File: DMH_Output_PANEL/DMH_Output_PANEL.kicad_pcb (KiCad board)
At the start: 2 copper layers, 50 x 200 mm, 17 parts, among them J0 Panel_GND_Solder_Wire_Pad

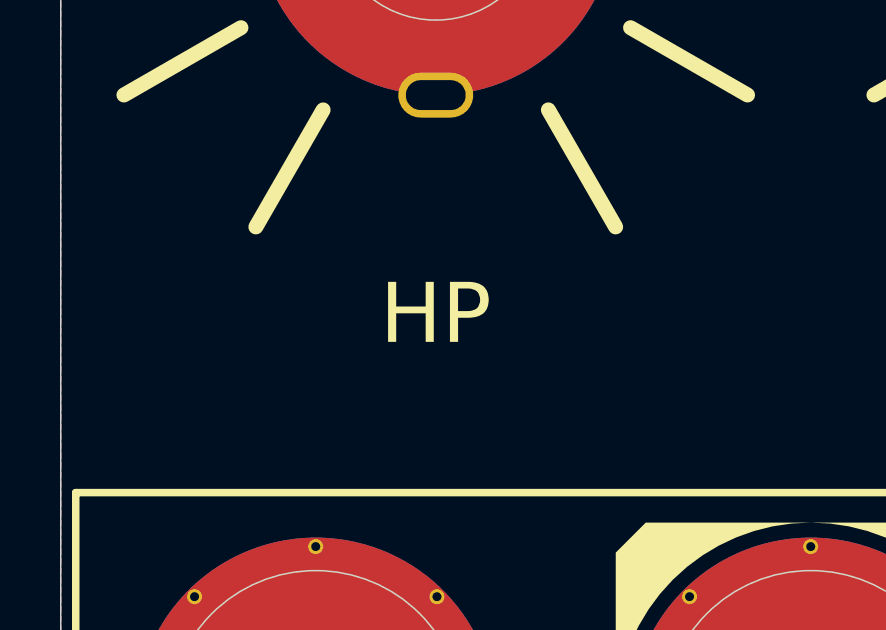
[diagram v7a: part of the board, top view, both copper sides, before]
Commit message: Generated Gerbers for prototyping
Panel, Controls and LEDs only
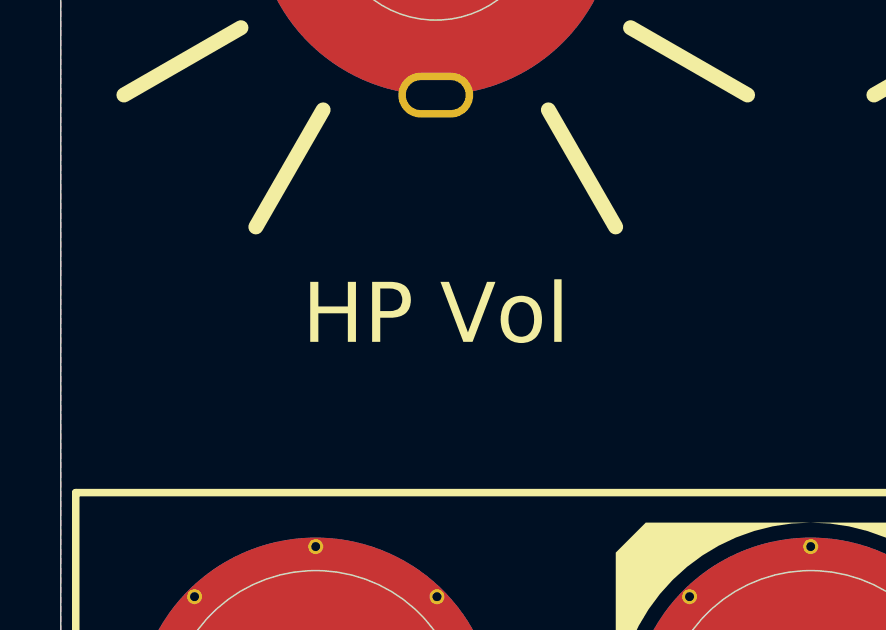
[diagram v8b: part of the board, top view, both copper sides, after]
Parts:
- H14: value HP -> HP Vol
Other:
- board text added: "Mk1.0 - March 2026"
- board text removed: "Mk1.0 - Month Year"
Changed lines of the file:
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@@
 			(plot_on_all_layers_selection 0x00000000_00000000_00000000_00000000)
 			(disableapertmacros no)
-			(usegerberextensions no)
+			(usegerberextensions yes)
 			(usegerberattributes yes)
 			(usegerberadvancedattributes yes)
@@
 			(sketchdnponfab yes)
 			(crossoutdnponfab yes)
-			(subtractmaskfromsilk no)
+			(subtractmaskfromsilk yes)
 			(outputformat 1)
 			(mirror no)
-			(drillshape 1)
+			(drillshape 0)
 			(scaleselection 1)
-			(outputdirectory "")
+			(outputdirectory "Gerbers/")
 		)
 	)
@@
 			)
 		)
-		(property "Value" "HP"
+		(property "Value" "HP Vol"
 			(at 0 13.3 0)
 			(unlocked yes)
@@
 				)
 			)
-			(render_cache "HP" 0
+			(render_cache "HP Vol" 0
 				(polygon
 					(pts
-						(xy 61.883287 157.238583) (xy 61.883287 157.926371) (xy 60.754885 157.926371) (xy 60.754885 157.238583)
-						(xy 60.245272 157.238583) (xy 60.245272 159.13) (xy 60.754885 159.13) (xy 60.754885 158.4024)
-						(xy 61.883287 158.4024) (xy 61.883287 159.13) (xy 62.392778 159.13) (xy 62.392778 157.238583)
-					)
-				)
-				(polygon
-					(pts
-						(xy 64.217401 157.249453) (xy 64.299066 157.264902) (xy 64.373438 157.286626) (xy 64.442917 157.315156)
-						(xy 64.505847 157.34957) (xy 64.567611 157.393281) (xy 64.623081 157.443014) (xy 64.697914 157.531132)
-						(xy 64.772332 157.661146) (xy 64.81781 157.801712) (xy 64.833008 157.946032) (xy 64.831956 157.983887)
-						(xy 64.823712 158.058421) (xy 64.807618 158.131076) (xy 64.783462 158.202888) (xy 64.751957 158.27162)
-						(xy 64.713217 158.337193) (xy 64.6679 158.398492) (xy 64.629296 158.441013) (xy 64.520744 158.530127)
-						(xy 64.459339 158.565895) (xy 64.391985 158.596097) (xy 64.318491 158.620306) (xy 64.238497 158.638165)
-						(xy 64.150207 158.649399) (xy 64.054606 158.653237) (xy 63.18388 158.653237) (xy 63.18388 159.13)
-						(xy 62.677076 159.13) (xy 62.677076 157.778848) (xy 63.18388 157.778848) (xy 63.18388 158.188443)
-						(xy 64.065841 158.188443) (xy 64.135466 158.183348) (xy 64.181423 158.172341) (xy 64.219982 158.155599)
-						(xy 64.255514 158.130522) (xy 64.284194 158.099295) (xy 64.314315 158.046432) (xy 64.325222 158.00797)
-						(xy 64.329013 157.965572) (xy 64.31977 157.897764) (xy 64.304156 157.858598) (xy 64.281385 157.823422)
-						(xy 64.249375 157.792248) (xy 64.215983 157.770819) (xy 64.175734 157.754504) (xy 64.125514 157.743672)
-						(xy 64.065841 157.739891) (xy 63.220272 157.739891) (xy 63.198281 157.745245) (xy 63.187634 157.757832)
-						(xy 63.18388 157.778848) (xy 62.677076 157.778848) (xy 62.677076 157.356186) (xy 62.690204 157.292338)
-						(xy 62.705763 157.270423) (xy 62.727241 157.254214) (xy 62.75981 157.242491) (xy 62.800297 157.238583)
-						(xy 64.054606 157.238583)
+						(xy 57.73702 157.238583) (xy 57.73702 157.926371) (xy 56.608618 157.926371) (xy 56.608618 157.238583)
+						(xy 56.099005 157.238583) (xy 56.099005 159.13) (xy 56.608618 159.13) (xy 56.608618 158.4024)
+						(xy 57.73702 158.4024) (xy 57.73702 159.13) (xy 58.246511 159.13) (xy 58.246511 157.238583)
+					)
+				)
+				(polygon
+					(pts
+						(xy 60.071134 157.249453) (xy 60.152799 157.264902) (xy 60.227171 157.286626) (xy 60.29665 157.315156)
+						(xy 60.35958 157.34957) (xy 60.421344 157.393281) (xy 60.476814 157.443014) (xy 60.551647 157.531132)
+						(xy 60.626065 157.661146) (xy 60.671543 157.801712) (xy 60.686741 157.946032) (xy 60.685689 157.983887)
+						(xy 60.677445 158.058421) (xy 60.661351 158.131076) (xy 60.637195 158.202888) (xy 60.60569 158.27162)
+						(xy 60.56695 158.337193) (xy 60.521633 158.398492) (xy 60.483029 158.441013) (xy 60.374477 158.530127)
+						(xy 60.313072 158.565895) (xy 60.245718 158.596097) (xy 60.172224 158.620306) (xy 60.09223 158.638165)
+						(xy 60.00394 158.649399) (xy 59.908339 158.653237) (xy 59.037613 158.653237) (xy 59.037613 159.13)
+						(xy 58.530809 159.13) (xy 58.530809 157.778848) (xy 59.037613 157.778848) (xy 59.037613 158.188443)
+						(xy 59.919574 158.188443) (xy 59.989199 158.183348) (xy 60.035156 158.172341) (xy 60.073715 158.155599)
+						(xy 60.109247 158.130522) (xy 60.137927 158.099295) (xy 60.168048 158.046432) (xy 60.178955 158.00797)
+						(xy 60.182746 157.965572) (xy 60.173503 157.897764) (xy 60.157889 157.858598) (xy 60.135118 157.823422)
+						(xy 60.103108 157.792248) (xy 60.069716 157.770819) (xy 60.029467 157.754504) (xy 59.979247 157.743672)
+						(xy 59.919574 157.739891) (xy 59.074005 157.739891) (xy 59.052014 157.745245) (xy 59.041367 157.757832)
+						(xy 59.037613 157.778848) (xy 58.530809 157.778848) (xy 58.530809 157.356186) (xy 58.543937 157.292338)
+						(xy 58.559496 157.270423) (xy 58.580974 157.254214) (xy 58.613543 157.242491) (xy 58.65403 157.238583)
+						(xy 59.908339 157.238583)
+					)
+				)
+				(polygon
+					(pts
+						(xy 62.645813 158.822254) (xy 62.682259 158.893246) (xy 62.723624 158.955918) (xy 62.766746 159.006923)
+						(xy 62.814386 159.050835) (xy 62.864797 159.086575) (xy 62.919637 159.115819) (xy 63.043699 159.155194)
+						(xy 63.194627 159.169078) (xy 63.278259 159.165156) (xy 63.355294 159.153334) (xy 63.420894 159.135292)
+						(xy 63.481268 159.110352) (xy 63.534538 159.079831) (xy 63.583348 159.042821) (xy 63.668607 158.948673)
+						(xy 63.740509 158.822254) (xy 64.418161 157.322602) (xy 64.448936 157.238583) (xy 63.858112 157.238583)
+						(xy 63.835764 157.30575) (xy 63.275715 158.612327) (xy 63.258407 158.642458) (xy 63.238232 158.660856)
+						(xy 63.197313 158.671067) (xy 63.170101 158.666974) (xy 63.145665 158.65395) (xy 63.116225 158.612327)
+						(xy 62.550558 157.30575) (xy 62.531019 157.238583) (xy 61.931769 157.238583) (xy 61.962543 157.322602)
+					)
+				)
+				(polygon
+					(pts
+						(xy 65.810575 157.239181) (xy 65.910967 157.245892) (xy 66.005315 157.259784) (xy 66.094384 157.280683)
+						(xy 66.177697 157.308169) (xy 66.257368 157.342845) (xy 66.331381 157.383713) (xy 66.403107 157.432792)
+						(xy 66.469068 157.487833) (xy 66.538587 157.559281) (xy 66.639786 157.698198) (xy 66.713915 157.851781)
+						(xy 66.759062 158.015176) (xy 66.77425 158.184413) (xy 66.774219 158.192301) (xy 66.769512 158.281359)
+						(xy 66.757053 158.367822) (xy 66.736781 158.452793) (xy 66.709228 158.534326) (xy 66.674311 158.612971)
+						(xy 66.632715 158.687313) (xy 66.584634 158.757226) (xy 66.530617 158.822009) (xy 66.439677 158.909144)
+						(xy 66.303848 159.00255) (xy 66.228868 159.040063) (xy 66.148554 159.071466) (xy 66.062703 159.096487)
+						(xy 65.971317 159.114783) (xy 65.873122 159.126144) (xy 65.769068 159.13) (xy 65.371441 159.13)
+						(xy 65.228524 159.122602) (xy 65.133867 159.108653) (xy 65.044779 159.087823) (xy 64.960533 159.06017)
+						(xy 64.881754 159.026135) (xy 64.80671 158.985027) (xy 64.737187 158.937887) (xy 64.670669 158.882846)
+						(xy 64.609892 158.822009) (xy 64.598805 158.809677) (xy 64.499477 158.673674) (xy 64.426299 158.52126)
+						(xy 64.38144 158.356905) (xy 64.366495 158.1871) (xy 64.873063 158.1871) (xy 64.882912 158.279528)
+						(xy 64.899443 158.336916) (xy 64.923252 158.390905) (xy 64.953891 158.441015) (xy 64.990666 158.486297)
+						(xy 65.016607 158.512471) (xy 65.107485 158.575764) (xy 65.162012 158.59921) (xy 65.223115 158.616621)
+						(xy 65.293374 158.627793) (xy 65.371441 158.631622) (xy 65.769068 158.631622) (xy 65.81519 158.63033)
+						(xy 65.886382 158.622582) (xy 65.950488 158.60821) (xy 66.008478 158.587383) (xy 66.060001 158.560665)
+						(xy 66.108121 158.526295) (xy 66.149843 158.486297) (xy 66.20821 158.40733) (xy 66.252482 158.300684)
+						(xy 66.267446 158.1871) (xy 66.267366 158.178682) (xy 66.26214 158.118558) (xy 66.2491 158.06057)
+						(xy 66.228415 158.004675) (xy 66.200741 157.95245) (xy 66.127495 157.862868) (xy 66.121897 157.857747)
+						(xy 66.031362 157.79479) (xy 65.978613 157.771905) (xy 65.918972 157.754813) (xy 65.848773 157.74371)
+						(xy 65.769068 157.739891) (xy 65.371441 157.739891) (xy 65.233063 157.752381) (xy 65.170952 157.768752)
+						(xy 65.116179 157.791226) (xy 65.061222 157.823763) (xy 65.013015 157.862868) (xy 65.003919 157.871628)
+						(xy 64.965226 157.91557) (xy 64.93259 157.964483) (xy 64.888089 158.07238) (xy 64.873063 158.1871)
+						(xy 64.366495 158.1871) (xy 64.366259 158.184413) (xy 64.370407 158.095581) (xy 64.382577 158.009061)
+						(xy 64.4024 157.925118) (xy 64.430108 157.842581) (xy 64.464994 157.763541) (xy 64.507181 157.687571)
+						(xy 64.555903 157.616029) (xy 64.671441 157.487833) (xy 64.704831 157.458664) (xy 64.840363 157.365355)
+						(xy 64.914603 157.328084) (xy 64.994269 157.296811) (xy 65.079221 157.271962) (xy 65.169926 157.253747)
+						(xy 65.267561 157.242432) (xy 65.371441 157.238583) (xy 65.769068 157.238583)
+					)
+				)
+				(polygon
+					(pts
+						(xy 68.988555 159.13) (xy 68.988555 158.645666) (xy 67.675384 158.645666) (xy 67.614378 158.641469)
+						(xy 67.569166 158.627719) (xy 67.546109 158.611698) (xy 67.529054 158.589693) (xy 67.510445 158.525847)
+						(xy 67.507345 158.466636) (xy 67.507345 157.238583) (xy 66.997732 157.238583) (xy 66.997732 158.514141)
+						(xy 67.00177 158.62339) (xy 67.014403 158.721939) (xy 67.03215 158.796207) (xy 67.056921 158.862998)
+						(xy 67.08521 158.916102) (xy 67.119731 158.963309) (xy 67.158235 159.002387) (xy 67.202823 159.036243)
+						(xy 67.311104 159.088236) (xy 67.45392 159.120433) (xy 67.613712 159.13)
 					)
 				)
@@
 		)
 	)
-	(gr_text "Mk1.0 - Month Year"
+	(gr_text "Mk1.0 - March 2026"
 		(at 75 222.95 0)
 		(layer "B.SilkS")
